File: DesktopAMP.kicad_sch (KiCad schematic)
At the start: 4 parts, among them U1 PCM5222

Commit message: WIP
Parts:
- added C? (x19): 10uF, symbol Device:C
- added C?: 680uF, symbol Device:C_Polarized
- added C?: 220uF, symbol Device:C_Polarized
- added D?: LED, symbol Device:LED
- added D?: 1N5822, Diode_THT:D_DO-201AD_P15.24mm_Horizontal, symbol Diode:1N5822
- added L?: 33uH, symbol Device:L
- added R?: 1K, symbol Device:R
- added R? (x10): R, symbol Device:R
- added U?: AT24CS01-STUM, Package_TO_SOT_SMD:SOT-23-5, symbol Memory_EEPROM:AT24CS01-STUM
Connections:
- net AVDD: now also U1.14 (AVDD), U1.5 (CPVDD), U?.2 (VO), C?.1, C?.1, C?.1, C?.1, C?.1, C?.1, C?.1
- net DVDD: now also U1.4 (DVDD), U?.2 (VO), C?.1, C?.1, R?.1, R?.1, R?.2, R?.2, U?.4 (VCC)
- net VINP: now reaches U?.1 (VIN)
- net VINP: now also C?.1
- net at U?.2 (OUT): now also D?.1 (K), L?.1
- net GND: now reaches U?.3 (GND)
- net GND: now also U1.15 (AGND), U1.16 (VCOM), U1.3 (DGND), U1.33 (EPAD), U?.1 (GND), U?.1 (GND), U?.5 (ON/OFF), C?.2, C?.2, C?.2, C?.2, C?.2, C?.2, C?.2, C?.2, C?.2, C?.2, C?.2, C?.2, C?.2, C?.2, C?.2, D?.2 (A), R?.2, U?.2 (GND)
- net 5V: now reaches U?.4 (Feedback)
- net 5V: now also U?.3 (VI), U?.3 (VI), C?.1, C?.1, C?.1, L?.2
- net at U1.1 (XSMT): now also U1.24 (MODE2), U1.32 (ADR1), R?.1
- net at U1.10 (OUTLP): now also R?.2
- net at U1.11 (OUTLN): now also R?.2
- net at U1.12 (OUTRN): now also R?.2
- net at U1.13 (OUTRP): now also R?.2
- net SDA: now reaches U1.17 (SDA)
- net SCL: now reaches U1.18 (SCL)
- net at U1.2 (LDOO): now also C?.1, C?.1
- net at U1.20 (GPIO4): now also D?.2 (A)
- net at U1.22 (ADR2): now also U1.23 (MODE1)
- net at U1.27 (BCK): now also R?.1
- net at U1.31 (LRCK): now also R?.1
- net at U1.6 (CAPP): now also C?.1
- net at U1.7 (CPGND): now also C?.1, C?.2, C?.2, C?.2, C?.2
- net at U1.8 (CAPM): now also C?.2
- net at U1.9 (VNEG): now also C?.2
- new net: R?.1, U?.5 (WP)
- new net: D?.1 (K), R?.1
- new net ID_SCL: R?.2, U?.1 (SCL)
- new net ID_SDA: R?.2, U?.3 (SDA)
- new net OUTL+: C?.1, R?.1
- new net OUTL-: C?.1, R?.1
- new net OUTR+: C?.1, R?.1
- new net OUTR-: C?.1, R?.1
- no-connect marks 0 -> 2
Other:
- moved on the sheet: U?

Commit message: WIP
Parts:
- removed C?: 10uF, symbol Device:C
- added C? (x2): C, symbol Device:C
- added C?: 10uF, symbol Device:C
- added J?: Conn_02x20_Odd_Even, symbol Connector_Generic:Conn_02x20_Odd_Even
- added R? (x3): 100R, symbol Device:R
- added R? (x2): 10K, symbol Device:R
- added X1: 22.5792MHz, Oscillator:Oscillator_SMD_EuroQuartz_XO53-4Pin_5.0x3.2mm, symbol Oscillator:XO53
- added X2: 24.5760MHz, Oscillator:Oscillator_SMD_EuroQuartz_XO53-4Pin_5.0x3.2mm, symbol Oscillator:XO53
- U1: value PCM5222 -> PCM5242
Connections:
- net 5V: now also C?.1
- net DVDD: now also C?.2, C?.2, C?.2, X1.4 (V+), X2.4 (V+); no longer C?.1
- net GND: now also C?.1, C?.1, C?.1, C?.2, J?.14 (Pin_14), J?.20 (Pin_20), J?.25 (Pin_25), J?.34 (Pin_34), J?.39 (Pin_39), J?.6 (Pin_6), J?.9 (Pin_9), R?.1, R?.1, X1.2 (GND), X2.2 (GND); no longer C?.2
- net SCL: now also J?.5 (Pin_5)
- net SDA: now also J?.3 (Pin_3)
- net GPIO3: now reaches U1.21 (GPIO3)
- net GPIO3: now also R?.2, X2.1 (EN)
- net GPIO6: now reaches U1.25 (GPIO6)
- net GPIO6: now also R?.2, X1.1 (EN)
- net CLK: now reaches U1.26 (SCK)
- net CLK: now also R?.2, R?.2
- net at U1.28 (DIN): now also R?.2
- net at U1.31 (LRCK): now also R?.2; no longer R?.1
- net BCK: now reaches R?.2
- net BCK: now also J?.12 (Pin_12)
- net ID_SCL renamed ID_SC
- net ID_SC: now also J?.28 (Pin_28)
- net ID_SDA renamed ID_SD
- net ID_SD: now also J?.27 (Pin_27)
- new net: R?.1, X1.3 (OUT)
- new net: J?.2 (Pin_2), J?.4 (Pin_4)
- new net: R?.1, X2.3 (OUT)
- new net DIN: J?.40 (Pin_40), R?.1
- new net LRCK: J?.35 (Pin_35), R?.1
- no-connect marks 2 -> 1
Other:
- moved on the sheet: C?, D?, L?, R?, U1, U?

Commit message: Added LM4780.
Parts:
- removed C? (x2): 10uF, symbol Device:C
- added C?: 10uF, symbol Device:C
- added C? (x4): C_Polarized, symbol Device:C_Polarized
- added C?: 1uF, symbol Device:C
- added C?: 100nF, symbol Device:C
- added R?: 10K, symbol Device:R
- added R? (x6): R, symbol Device:R
- added U? (x2): LM4780, symbol Etnolit:LM4780
- C? (x3): value 10uF -> 2.2uF
- C? (x2): value 10uF -> 100nF
- R?: value R -> 10K
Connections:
- net OUTL- is gone; now on net GND: C?.1, R?.1
- net OUTR- is gone; now on net GND: C?.1, R?.1
- net DVDD: now also C?.1, C?.1
- net GND: now also C?.1, C?.2, C?.2, U1.22 (ADR2), U1.23 (MODE1), U1.7 (CPGND), C?.2, C?.2, C?.2, C?.2, C?.2, U?.12 (GND), U?.19 (GND); no longer U1.16 (VCOM)
- net OUTL+: now also R?.1
- net OUTR+: now also R?.1
- net at R?.1, U1.24 (MODE2), U1.32 (ADR1): no longer U1.1 (XSMT)
- net 5VBK: now reaches J?.2 (Pin_2), J?.4 (Pin_4)
- net VINP renamed VCC
- net VCC: now also C?.1
- new net: C?.1, R?.1 (x2)
- new net: R?.1, R?.2, U?.15 (-)
- new net: C?.1, U1.16 (VCOM)
- new net: R?.2, U?.16 (+)
- new net: C?.2, U?.17 (V+), U?.27 (V+), U?.5 (V+), U?.8 (V+), U?.9 (V+)
- new net: C?.1, U?.10 (V-), U?.11 (V-), U?.18 (V-), U?.2 (V-), U?.4 (V-)
- new net: R?.1, R?.2, U?.21 (-)
- new net: R?.2, U?.22 (+)
- new net MUTE: R?.1, U?.14 (MUTE), U?.20 (MUTE)
- new net VEE: C?.2, R?.2
- new net V_{out}L: R?.2, U?.7
- new net V_{out}R: R?.2, U?.25
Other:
- moved on the sheet: C?, R?

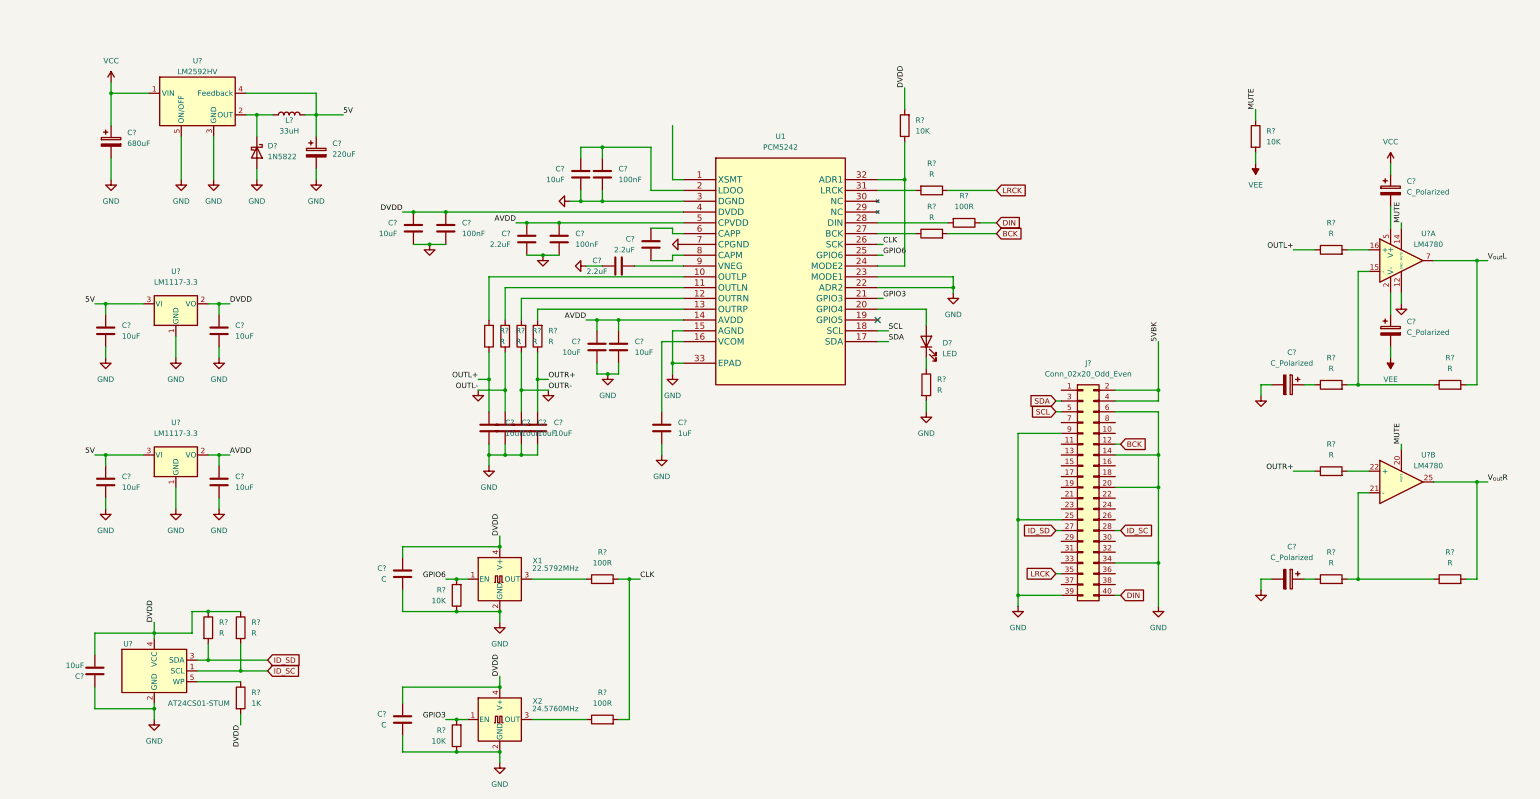
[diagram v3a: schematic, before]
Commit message: Added footprints to all components.
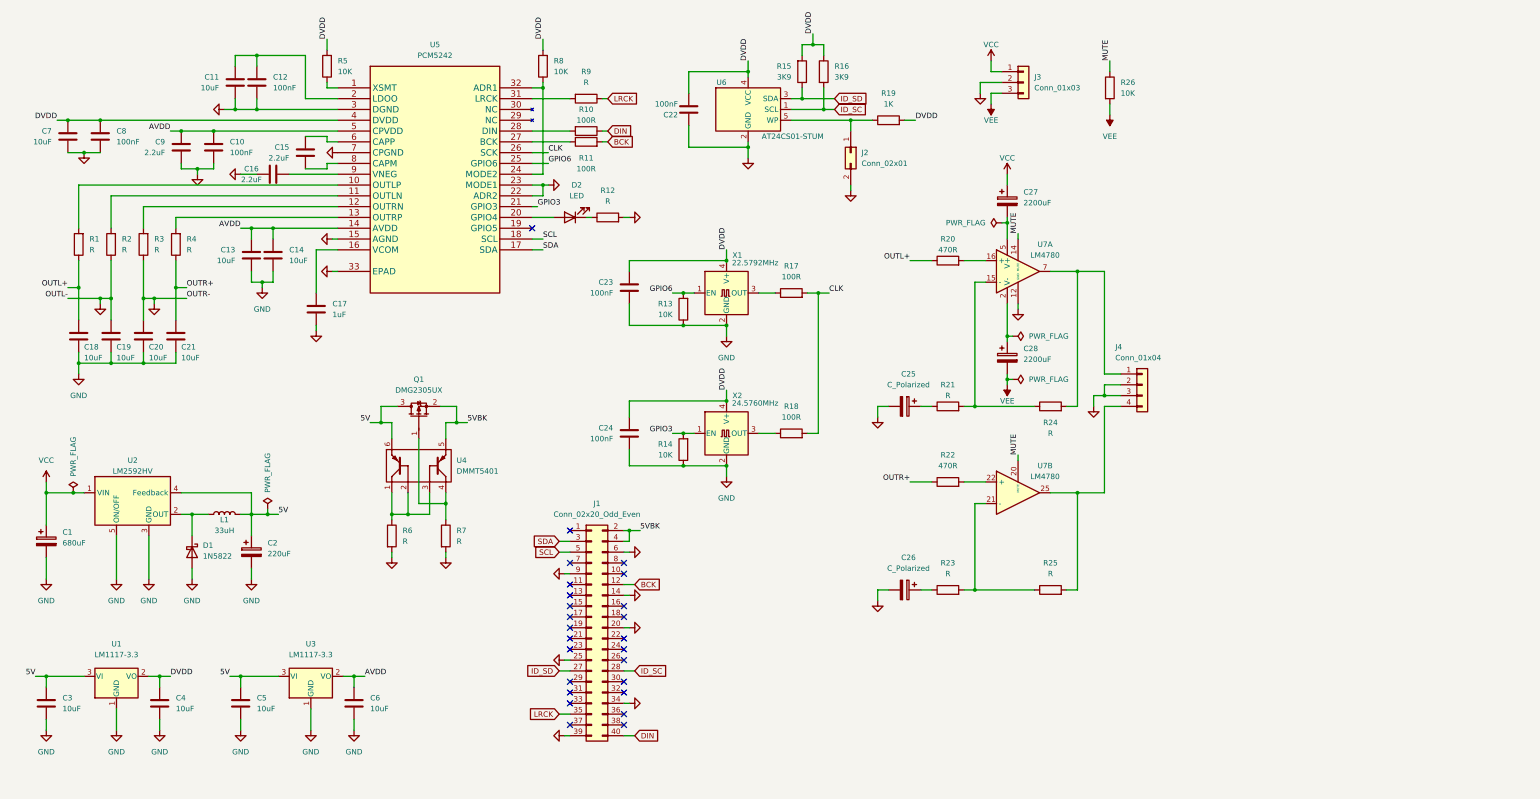
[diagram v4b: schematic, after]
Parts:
- added J2: Conn_02x01, Resistor_SMD:R_0805_2012Metric, symbol Connector_Generic:Conn_02x01
- added J3: Conn_01x03, Resistor_SMD:R_0805_2012Metric, symbol Connector_Generic:Conn_01x03
- added J4: Conn_01x04, Resistor_SMD:R_0805_2012Metric, symbol Connector_Generic:Conn_01x04
- added Q1: DMG2305UX, Resistor_SMD:R_0805_2012Metric, symbol Etnolit:DMG2305UX
- added R5: 10K, Resistor_SMD:R_0805_2012Metric, symbol Device:R
- added R6, R7: R, Resistor_SMD:R_0805_2012Metric, symbol Device:R
- added U4: DMMT5401, Package_TO_SOT_SMD:SOT-23-6, symbol Etnolit:DMMT5401
- C1: renamed from C?; footprint (none) -> Capacitor_THT:CP_Radial_D10.0mm_P3.50mm
- C10, C11, C12, C13, C14, C15, C16, C17, C18, C19, C20, C21, C3, C4, C5, C6, C7, C8, C9: renamed from C?; footprint (none) -> Capacitor_SMD:C_0805_2012Metric
- C2: renamed from C?; footprint (none) -> Capacitor_THT:CP_Radial_D8.0mm_P3.50mm
- C22: renamed from C?; value 10uF -> 100nF; footprint (none) -> Capacitor_SMD:C_0805_2012Metric
- C23, C24: renamed from C?; value C -> 100nF; footprint (none) -> Capacitor_SMD:C_0805_2012Metric
- C25, C26: renamed from C?; footprint (none) -> Capacitor_THT:CP_Radial_D6.3mm_P2.50mm
- C27, C28: renamed from C?; value C_Polarized -> 2200uF; footprint (none) -> Capacitor_THT:CP_Radial_D18.0mm_P7.50mm
- D2: renamed from D?; footprint (none) -> Resistor_SMD:R_0805_2012Metric
- J1: renamed from J?; footprint (none) -> Resistor_SMD:R_0805_2012Metric
- L1: renamed from L?; footprint (none) -> Resistor_SMD:R_0805_2012Metric
- R1, R10, R12, R13, R14, R17, R18, R19, R2, R21, R23, R24, R25, R26, R3, R4, R8, R9: renamed from R?; footprint (none) -> Resistor_SMD:R_0805_2012Metric
- R11: renamed from R?; value R -> 100R; footprint (none) -> Resistor_SMD:R_0805_2012Metric
- R15, R16: renamed from R?; value R -> 3K9; footprint (none) -> Resistor_SMD:R_0805_2012Metric
- R20, R22: renamed from R?; value R -> 470R; footprint (none) -> Resistor_SMD:R_0805_2012Metric
- U1, U3: renamed from U?; footprint (none) -> Package_TO_SOT_SMD:SOT-223-3_TabPin2
- U5: renamed from U1; symbol Etnolit:PCM5222 -> Etnolit:PCM5242RHB
- U7: renamed from U?; footprint (none) -> Etnolit:TO-220-27
- gave numbers to parts that had none: 3
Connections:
- net 5V: now also Q1.3, U4.6
- net 5VBK: now also Q1.2, U4.5
- net DVDD: now also R15.2, R5.2; no longer R15.1
- net GND: now also J2.2 (Pin_2), J3.2 (Pin_2), J4.2 (Pin_2), J4.3 (Pin_3), R6.2, R7.2
- net ID_SD: now also R15.1; no longer R15.2
- net VCC: now also J3.1 (Pin_1)
- net VEE: now also J3.3 (Pin_3)
- net at R19.1, U6.5 (WP): now also J2.1 (Pin_1)
- net at U5.1 (XSMT): now also R5.1
- net V_{out}L: no longer names the net of R24.2, U7.7
- net V_{out}L: now also J4.1 (Pin_1)
- net V_{out}R: no longer names the net of R25.2, U7.25
- net V_{out}R: now also J4.4 (Pin_4)
- new net: Q1.1, R7.1, U4.4
- new net: R6.1, U4.1, U4.2, U4.3
- no-connect marks 1 -> 25
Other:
- moved on the sheet: C1, C10, C11, C12, C13, C14, C15, C16, C17, C18, C19, C2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

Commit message: Footprints for all components.
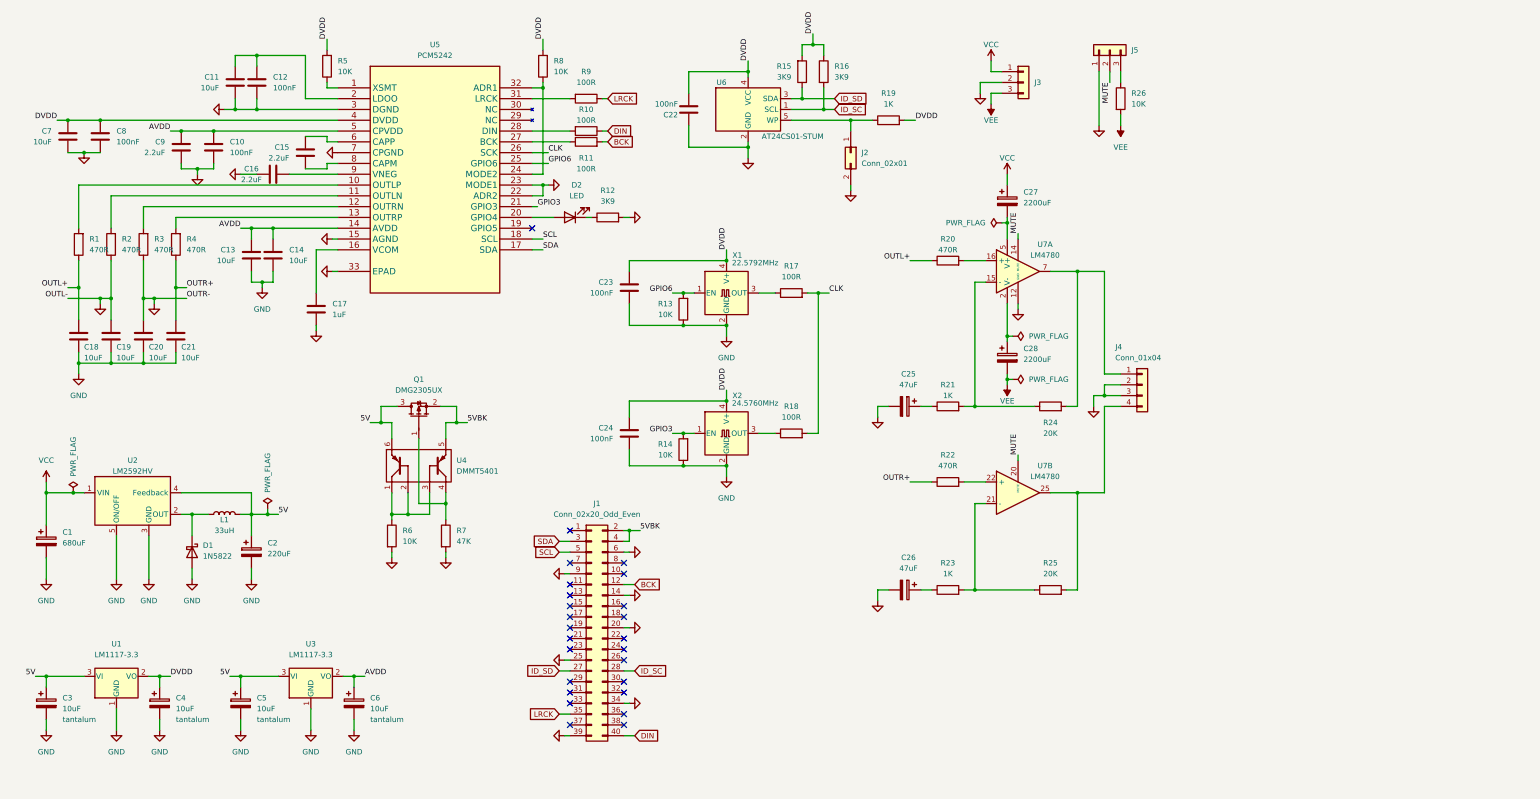
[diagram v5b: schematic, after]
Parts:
- added J5: Conn_01x03, Connector_PinHeader_2.54mm:PinHeader_1x03_P2.54mm_Vertical, symbol Connector_Generic:Conn_01x03
- C25, C26: value C_Polarized -> 47uF
- C3, C4, C5, C6: symbol Device:C -> Device:C_Polarized; Type (none) -> tantalum
- J1: footprint Resistor_SMD:R_0805_2012Metric -> Etnolit:Raspberry Pi Zero 2 W
- J3: footprint Resistor_SMD:R_0805_2012Metric -> Connector_Phoenix_MSTB:PhoenixContact_MSTBVA_2,5_3-G_1x03_P5.00mm_Vertical
- J4: footprint Resistor_SMD:R_0805_2012Metric -> Connector_Phoenix_MSTB:PhoenixContact_MSTBVA_2,5_4-G_1x04_P5.00mm_Vertical
- L1: footprint Resistor_SMD:R_0805_2012Metric -> Inductor_SMD:L_Bourns_SRR1260
- Q1: footprint Resistor_SMD:R_0805_2012Metric -> Package_TO_SOT_SMD:SOT-23
- R1, R2, R3, R4: value R -> 470R
- R12: value R -> 3K9
- R21, R23: value R -> 1K
- R24, R25: value R -> 20K
- R6: value R -> 10K
- R7: value R -> 47K
- R9: value R -> 100R
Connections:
- net GND: now also J5.1 (Pin_1)
- net MUTE: now also J5.2 (Pin_2); no longer R26.1
- new net: J5.3 (Pin_3), R26.1
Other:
- moved on the sheet: R26

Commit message: Worked on placement and footprints.
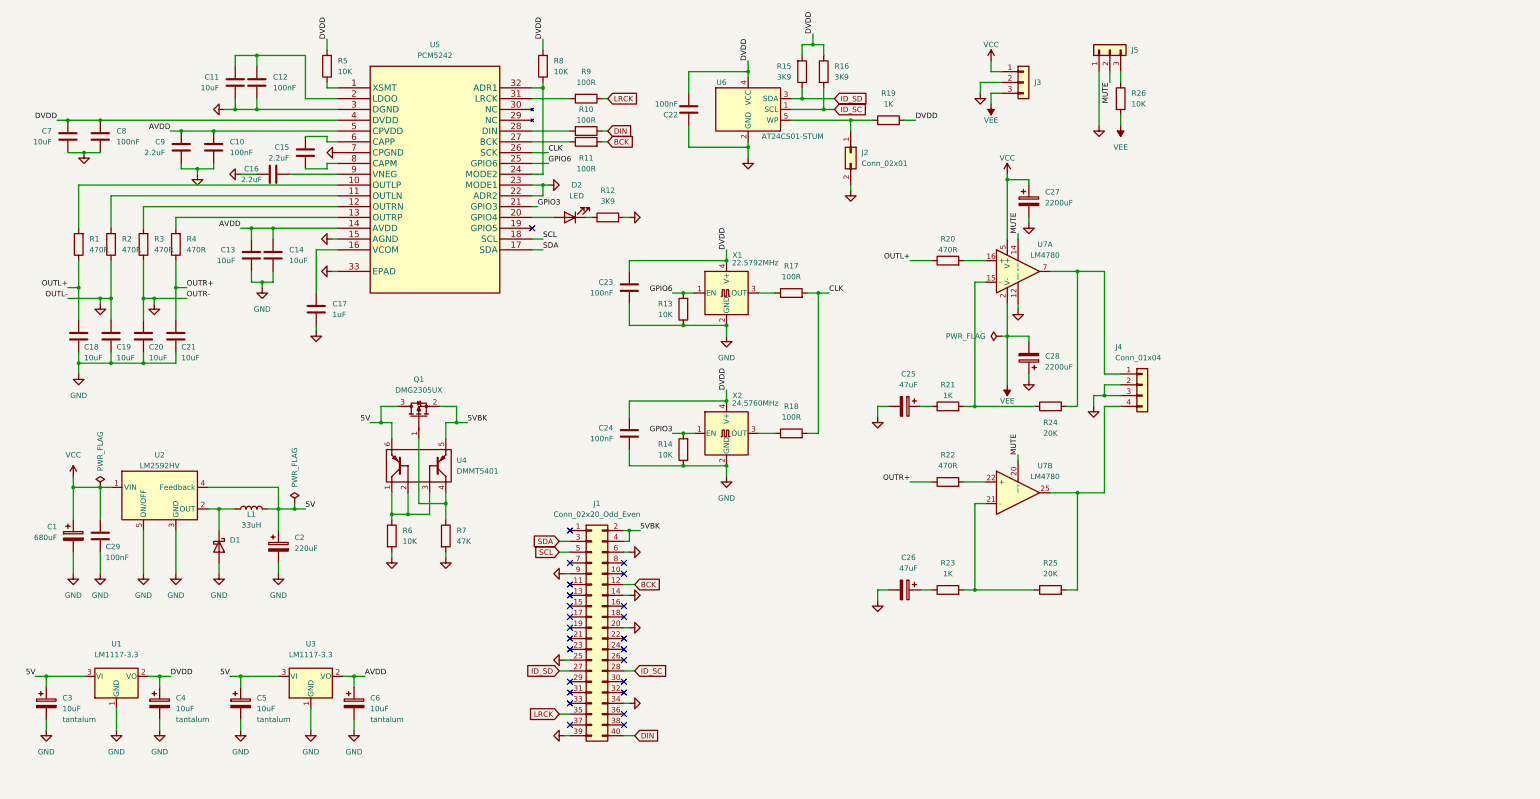
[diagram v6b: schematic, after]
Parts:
- added C29: 100nF, Capacitor_SMD:C_0805_2012Metric, symbol Device:C
- D1: value 1N5822 -> SSC54-E3/9AT; footprint Diode_THT:D_DO-201AD_P15.24mm_Horizontal -> Diode_SMD:D_SMC
- J1: footprint Etnolit:Raspberry Pi Zero 2 W -> Etnolit:RPi_Zero_2W
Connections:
- net GND: now also C27.2, C28.1, C29.2
- net VCC: now also U7.17 (V+), U7.27 (V+), U7.5 (V+), U7.8 (V+), U7.9 (V+), C29.1
- net VEE: now also U7.10 (V-), U7.11 (V-), U7.18 (V-), U7.2 (V-), U7.4 (V-)
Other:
- moved on the sheet: C1, C2, C27, C28, D1, L1, U2
